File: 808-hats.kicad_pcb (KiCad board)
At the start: 2 copper layers, 155 parts, among them J1 ohfilt-10k, J10 noisepresel, J11 noisein-pre, J12 noiseoutsrc, J2 chfilt-10k, J3 ohfilten, J4 chfilten, J5 trig/accent, J6 output, J7 noisesel, J8 noisein, J9 noiseout, P1 MTA-156-4, Q1 BC546, Q10 BC546, Q11 BC546, Q12 BC546, Q13 BC546, Q14 BC546, Q2 BC546, Q3 BC556, Q4 BC556, Q5 BC546, Q6 BC546, Q7 BC546, Q8 BC546, Q9 BC546, U1 40106, U2 TL074, U3 78L05, U4 TL072

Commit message: a lot more layout
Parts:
- moved R59 301.4 mm to (184.2, 58.7), turned to 90 degrees
- moved D2 292.5 mm to (176.3, 58.7), turned to 90 degrees
- moved R45 276.6 mm to (172.5, 69.3), turned to 180 degrees
- moved C20 272.9 mm to (166.4, 71.9)
- moved R49 271.9 mm to (164.8, 66.8)
- moved R48 270.6 mm to (153.2, 64.3), turned to 180 degrees
- moved R57 266.9 mm to (149.9, 58.7), turned to 90 degrees
- moved R56 263.2 mm to (142.0, 51.1), turned to 270 degrees
- moved Q14 262.9 mm to (175.5, 67.3)
- moved R51 261.1 mm to (164.8, 64.3)
- moved R44 259.4 mm to (153.2, 67.1), turned to 180 degrees
- moved R37 258.0 mm to (151.9, 80.0)
- moved R41 255.2 mm to (151.9, 77.5)
- moved R58 254.4 mm to (158.5, 51.1), turned to 270 degrees
- moved R33 253.6 mm to (159.5, 82.5), turned to 180 degrees
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
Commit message: more layout
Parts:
- moved P1 173.7 mm to (63.2, 60.2)
- moved L2 163.8 mm to (70.4, 56.6)
- moved L1 163.7 mm to (70.1, 75.7)
- moved D3 162.8 mm to (109.5, 115.8), turned to 90 degrees
- moved R64 162.6 mm to (88.6, 131.8)
- moved R70 145.0 mm to (91.7, 116.1)
- moved C35 144.9 mm to (105.4, 115.8), turned to 90 degrees
- moved R68 144.9 mm to (105.4, 118.9)
- moved R62 143.7 mm to (94.2, 110.7)
- moved R63 143.2 mm to (95.2, 124.5)
- moved C36 141.6 mm to (106.4, 127.3), turned to 90 degrees
- moved D4 136.4 mm to (102.9, 127.3), turned to 180 degrees
- moved R69 135.4 mm to (110.2, 127.3)
- moved R71 133.9 mm to (85.1, 124.5)
- moved REF** 107.9 mm to (61.5, 130.0)
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
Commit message: squishing
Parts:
- moved R69 17.5 mm to (92.7, 126.7), turned to 180 degrees
- moved R19 17.2 mm to (90.4, 99.1)
- moved R48 13.6 mm to (129.0, 73.9)
- moved R44 13.4 mm to (129.0, 76.2)
- moved J5 10.9 mm to (115.3, 128.0)
- moved Q1 10.7 mm to (148.1, 89.4)
- moved Q13 10.7 mm to (138.9, 72.6)
- moved Q14 10.7 mm to (152.9, 72.6)
- moved R24 10.7 mm to (153.4, 81.8)
- moved R25 10.7 mm to (156.0, 89.4)
- moved R33 10.7 mm to (149.1, 84.8)
- moved R37 10.7 mm to (141.5, 82.3)
- moved R41 10.7 mm to (141.5, 79.8)
- moved R45 10.7 mm to (149.9, 74.7)
- moved R49 10.7 mm to (142.2, 72.1)
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
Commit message: much layout work
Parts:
- moved J5 99.5 mm to (205.7, 86.6), turned to 180 degrees
- moved R72 98.7 mm to (185.9, 79.8)
- moved R74 98.7 mm to (185.9, 77.5)
- moved R70 97.2 mm to (184.9, 88.6)
- moved R73 97.2 mm to (185.0, 93.2)
- moved R75 97.2 mm to (185.0, 91.0)
- moved C36 96.9 mm to (199.4, 99.8)
- moved C10 96.0 mm to (164.1, 78.2)
- moved C35 96.0 mm to (197.4, 88.4)
- moved D4 96.0 mm to (194.8, 98.0)
- moved R63 96.0 mm to (187.2, 95.5)
- moved R67 96.0 mm to (161.5, 93.5)
- moved R68 96.0 mm to (197.4, 91.4)
- moved R9 96.0 mm to (166.1, 83.3)
- moved C11 96.0 mm to (169.2, 85.9)
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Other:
- board outline added: 152.4 x 50.8 mm

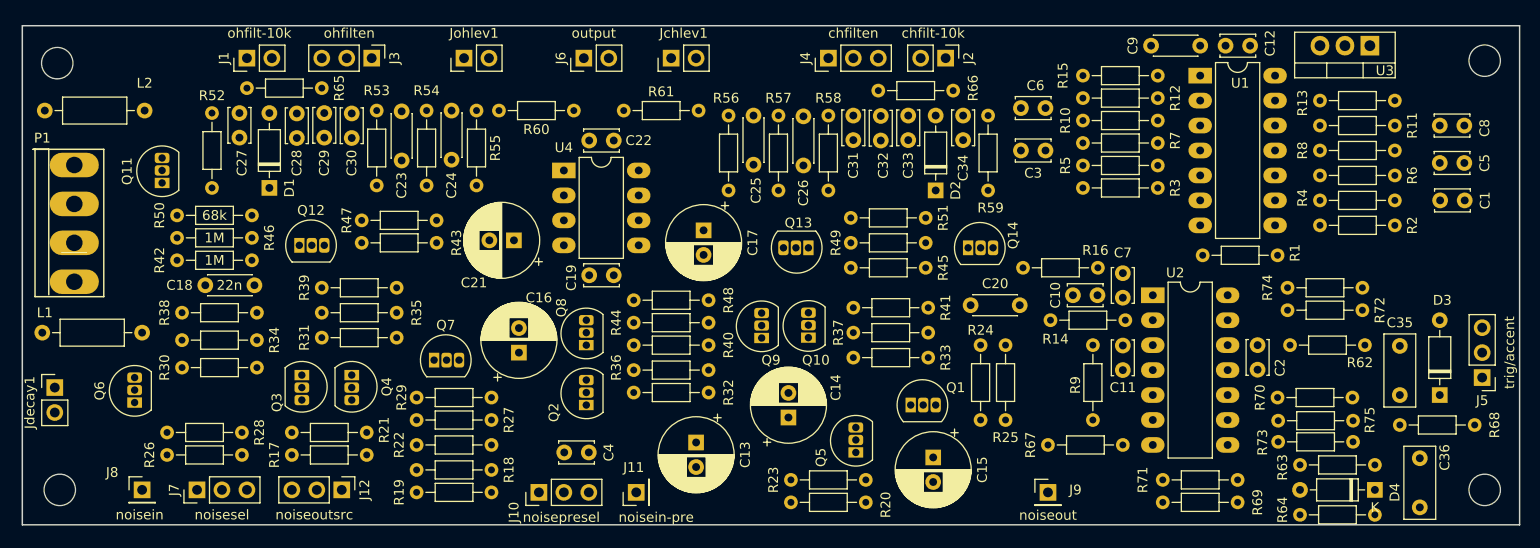
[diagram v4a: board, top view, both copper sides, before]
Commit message: exposed and moved around value labels
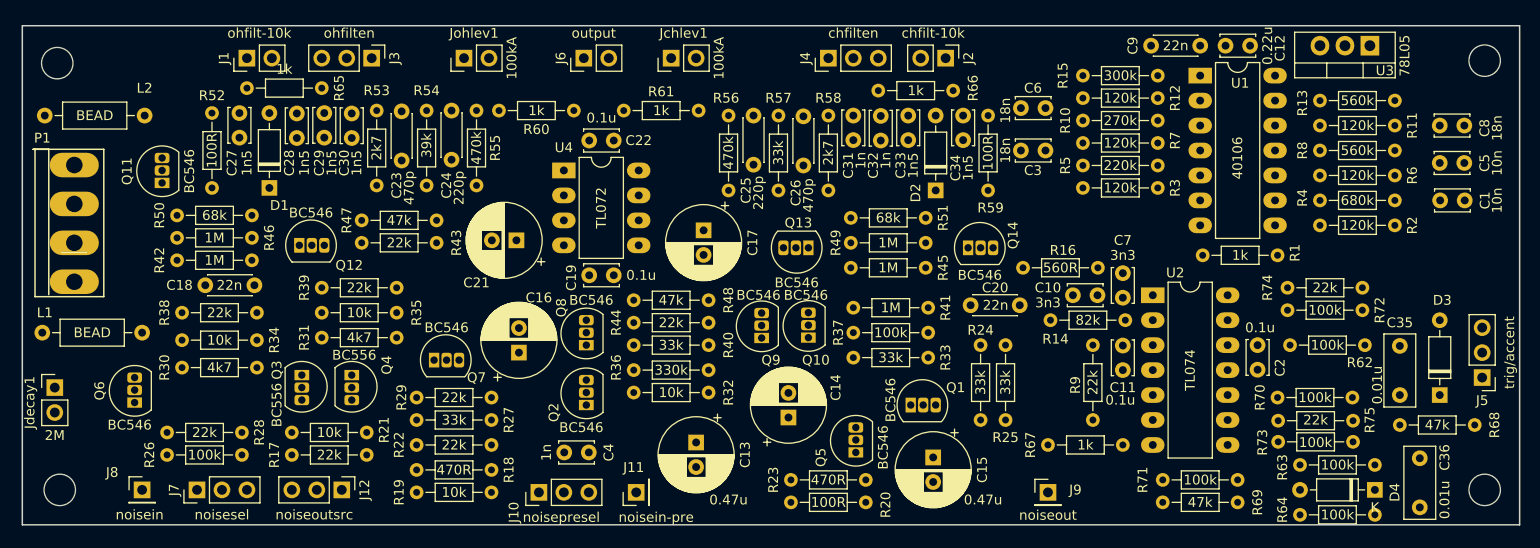
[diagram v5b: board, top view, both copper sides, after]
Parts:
- moved L2 0.51 mm to (69.6, 59.9)
- moved C21 0.25 mm to (107.4, 72.6)

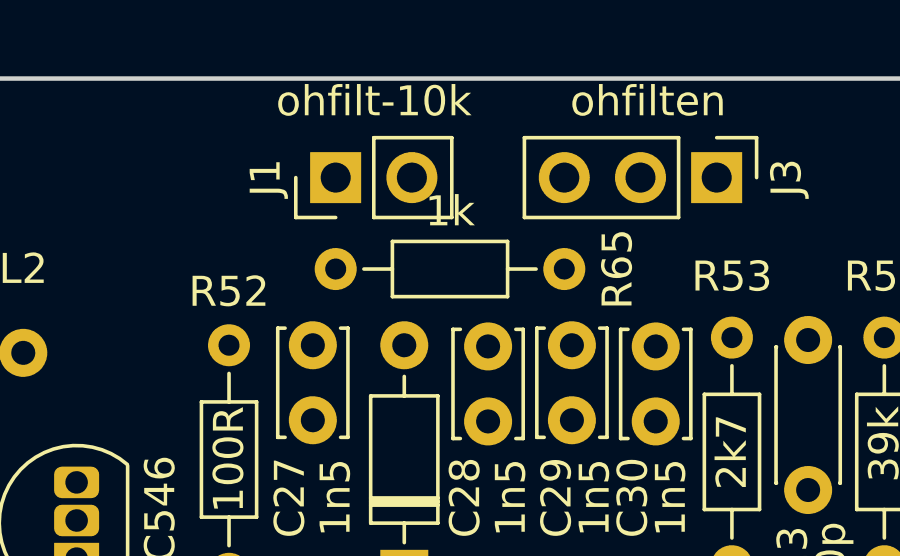
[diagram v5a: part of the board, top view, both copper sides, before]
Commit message: setup design rules
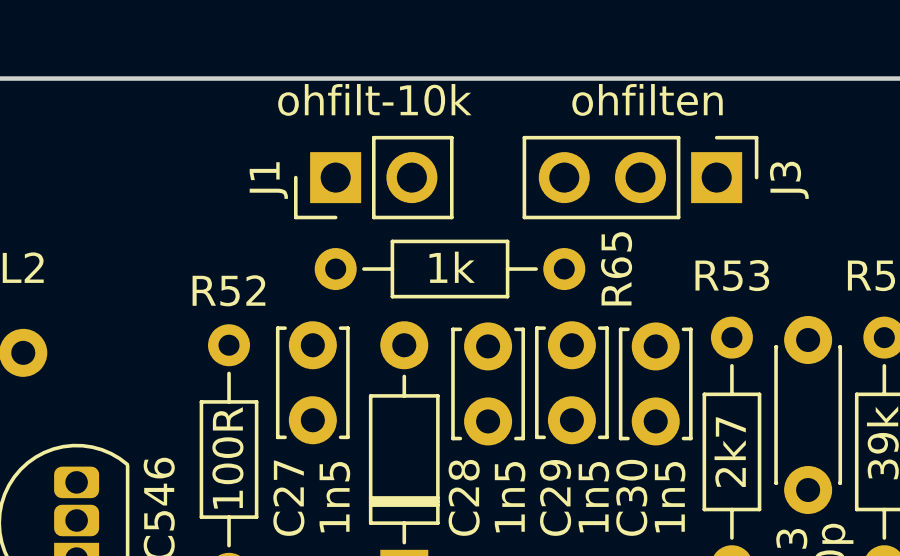
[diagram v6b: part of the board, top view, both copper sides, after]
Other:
- net class Default: clearance 0.2 -> 0.1524; trace_width 0.25 -> 0.1524; via_dia 0.8 -> 0.6858; via_drill 0.4 -> 0.3302
- rule trace_clearance: 0.2 -> 0.1524
- rule trace_min: 0.2 -> 0.1524
- rule via_min_drill: 0.3 -> 0.3302
- rule via_min_size: 0.4 -> 0.6858
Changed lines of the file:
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@@
   )
   (setup
-    (last_trace_width 0.25)
-    (trace_clearance 0.2)
+    (last_trace_width 0.1524)
+    (user_trace_width 0.1524)
+    (user_trace_width 0.3048)
+    (user_trace_width 0.381)
+    (user_trace_width 0.635)
+    (user_trace_width 0.762)
+    (trace_clearance 0.1524)
     (zone_clearance 0.508)
     (zone_45_only no)
-    (trace_min 0.2)
+    (trace_min 0.1524)
     (segment_width 0.2)
     (edge_width 0.15)
-    (via_size 0.8)
-    (via_drill 0.4)
-    (via_min_size 0.4)
-    (via_min_drill 0.3)
-    (uvia_size 0.3)
-    (uvia_drill 0.1)
+    (via_size 0.6858)
+    (via_drill 0.3302)
+    (via_min_size 0.6858)
+    (via_min_drill 0.3302)
+    (uvia_size 0.6858)
+    (uvia_drill 0.3302)
     (uvias_allowed no)
     (uvia_min_size 0.2)
@@
   (net 98 "Net-(R73-Pad1)")
   (net_class Default "This is the default net class."
-    (clearance 0.2)
-    (trace_width 0.25)
-    (via_dia 0.8)
-    (via_drill 0.4)
-    (uvia_dia 0.3)
-    (uvia_drill 0.1)
+    (clearance 0.1524)
+    (trace_width 0.1524)
+    (via_dia 0.6858)
+    (via_drill 0.3302)
+    (uvia_dia 0.6858)
+    (uvia_drill 0.3302)
+    (diff_pair_gap 0.1524)
+    (diff_pair_width 0.1524)
     (add_net +15V)
     (add_net +5V)
@@
     )
     (fp_line (start -1.27 8.89) (end 1.27 8.89) (layer F.SilkS) (width 0.15))
-    (fp_line (start 3.2 13.4) (end 3.2 -1.6) (layer F.CrtYd) (width 0.15))
-    (fp_line (start -4.2 13.6) (end 3.2 13.6) (layer F.CrtYd) (width 0.15))
-    (fp_line (start -4.2 -1.8) (end -4.2 13.4) (layer F.CrtYd) (width 0.15))
-    (fp_line (start 3.2 -1.8) (end -4.2 -1.8) (layer F.CrtYd) (width 0.15))
     (fp_line (start 3 13.4) (end -4 13.4) (layer F.SilkS) (width 0.15))
     (fp_line (start 3 -1.6) (end 3 13.4) (layer F.SilkS) (width 0.15))
@@
     (fp_line (start -4.2 -1.6) (end -2.6 -1.6) (layer F.SilkS) (width 0.15))
     (fp_line (start -4 -1.6) (end -4 13.4) (layer F.SilkS) (width 0.15))
+    (fp_line (start -4.191 -1.778) (end 3.175 -1.778) (layer F.CrtYd) (width 0.15))
+    (fp_line (start 3.175 -1.778) (end 3.175 13.589) (layer F.CrtYd) (width 0.15))
+    (fp_line (start 3.175 13.589) (end -4.191 13.589) (layer F.CrtYd) (width 0.15))
+    (fp_line (start -4.191 13.589) (end -4.191 -1.778) (layer F.CrtYd) (width 0.15))
     (pad 4 thru_hole oval (at 0 11.88) (size 5 2.5) (drill 1.68) (layers *.Cu *.Mask F.SilkS)
       (net 60 "Net-(L1-Pad2)"))
@@
       (effects (font (size 1 1) (thickness 0.15)))
     )
-    (fp_text value 1k (at 3.81 1.92 180) (layer F.SilkS)
+    (fp_text value 1k (at 3.81 0 180) (layer F.SilkS)
       (effects (font (size 1 1) (thickness 0.15)))
     )

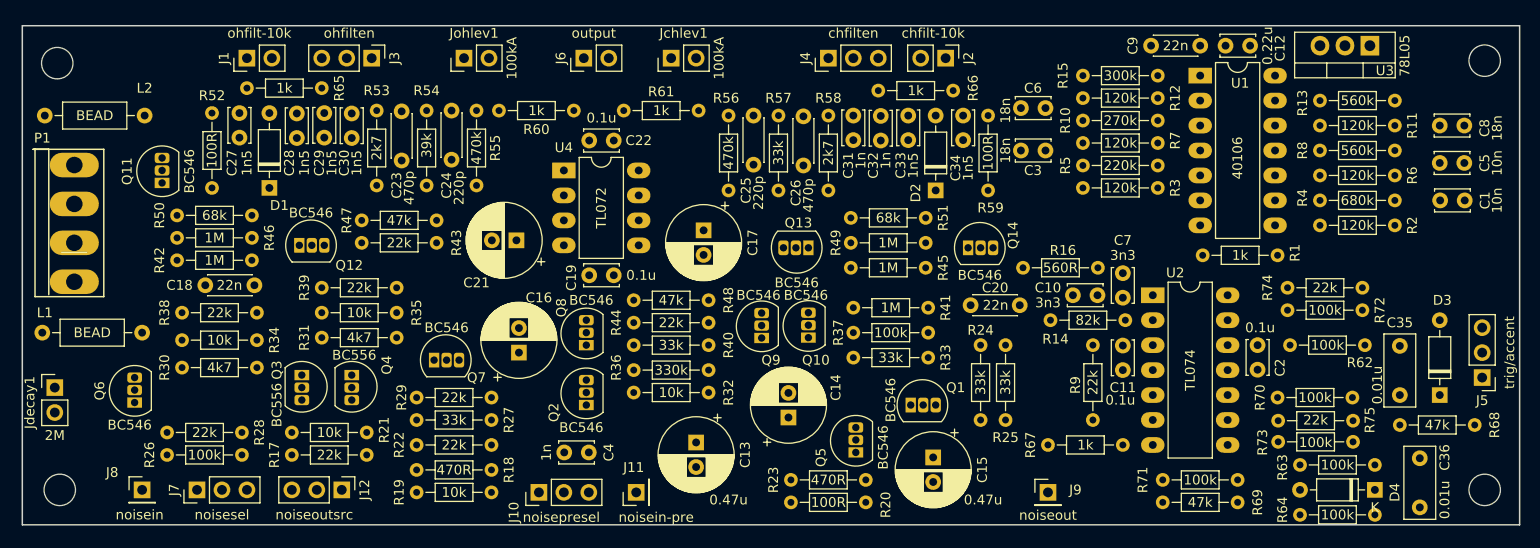
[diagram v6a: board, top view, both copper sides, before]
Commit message: fully routed, removed some i/o that could move onto switches
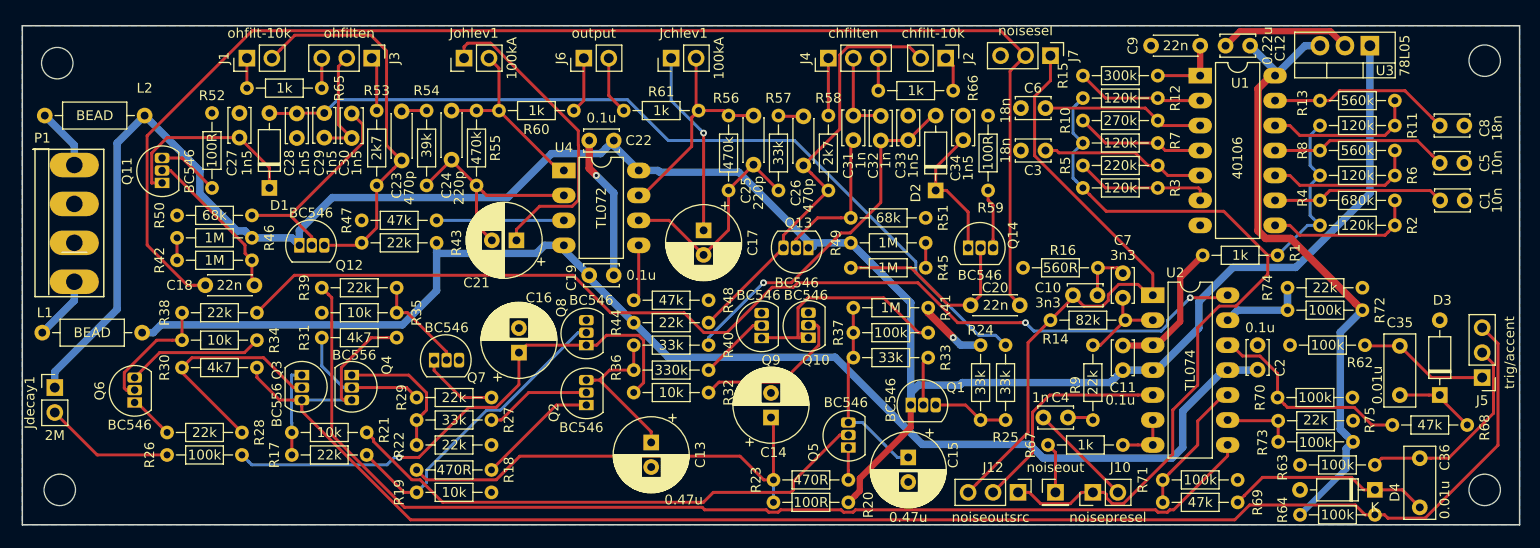
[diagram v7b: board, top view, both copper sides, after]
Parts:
- removed J11: noisein-pre, Connector_PinHeader_2.54mm:PinHeader_1x01_P2.54mm_Vertical
- removed J8: noisein, Connector_PinHeader_2.54mm:PinHeader_1x01_P2.54mm_Vertical
- J10: footprint Connector_PinHeader_2.54mm:PinHeader_1x03_P2.54mm_Vertical -> Connector_PinHeader_2.54mm:PinHeader_1x02_P2.54mm_Vertical
- moved J7 97.5 mm to (161.8, 53.8), turned to 270 degrees
- moved J12 68.8 mm to (158.5, 98.3)
- moved J10 56.4 mm to (166.1, 98.3)
- moved C4 48.9 mm to (163.6, 90.7)
- moved R68 6.86 mm to (204.2, 91.4), turned to 180 degrees
- moved C13 4.57 mm to (121.2, 93.2)
- moved C15 2.54 mm to (147.3, 94.7)
- moved C14 1.78 mm to (133.3, 90.7)
- moved R20 1.78 mm to (133.6, 99.3)
- moved R23 1.78 mm to (133.6, 97.0)
- moved Q5 0.92 mm to (141.2, 93.7)
- moved J9 0.76 mm to (162.3, 98.3)
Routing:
- net +15V: track 0.00 -> 226.2 mm
- net accent: track 0.00 -> 167.1 mm
- net noise: track 0.00 -> 140.1 mm
- net -15V: track 0.00 -> 135.9 mm
- net Net-(R39-Pad1): track 0.00 -> 113.7 mm
- net Net-(R38-Pad1): track 0.00 -> 108.7 mm, vias 0 -> 2
- net Net-(J10-Pad1): track 0.00 -> 95.6 mm
- net ohcnt: track 0.00 -> 86.5 mm
- net +5V: track 0.00 -> 65.2 mm
- net Net-(C10-Pad1): track 0.00 -> 64.8 mm
- net GND: track 0.00 -> 63.9 mm, vias 0 -> 2
- net Net-(Q5-Pad2): track 0.00 -> 55.4 mm
- net Net-(C16-Pad1): track 0.00 -> 54.6 mm, vias 0 -> 1
- net Net-(C14-Pad1): track 0.00 -> 47.5 mm
- net Net-(C26-Pad1): track 0.00 -> 43.9 mm
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- added copper zone on B.Cu, net GND

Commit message: labels, .. final layout?
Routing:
- net GND: track 63.9 -> 93.6 mm, vias 2 -> 7
- net -15V: track 135.9 -> 141.6 mm
- net Net-(R47-Pad2): track 13.0 -> 15.6 mm
- net Net-(C14-Pad1): track 47.5 -> 45.9 mm
- net +15V: track 226.2 -> 227.1 mm
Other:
- board text added: "808 Hats"
- board text added: "8Nov2020"
- board text added: "https://github.com/x37v/808-hats"
